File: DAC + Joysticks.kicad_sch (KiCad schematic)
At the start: 105 parts, among them J10 L Phono, J11 R Phono, J8 JOY0, J9 JOY1, U23 74HC374, U24 74HC374, U25 74LS244, U26 74LS244, U27 74LS373, U28 74LS244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

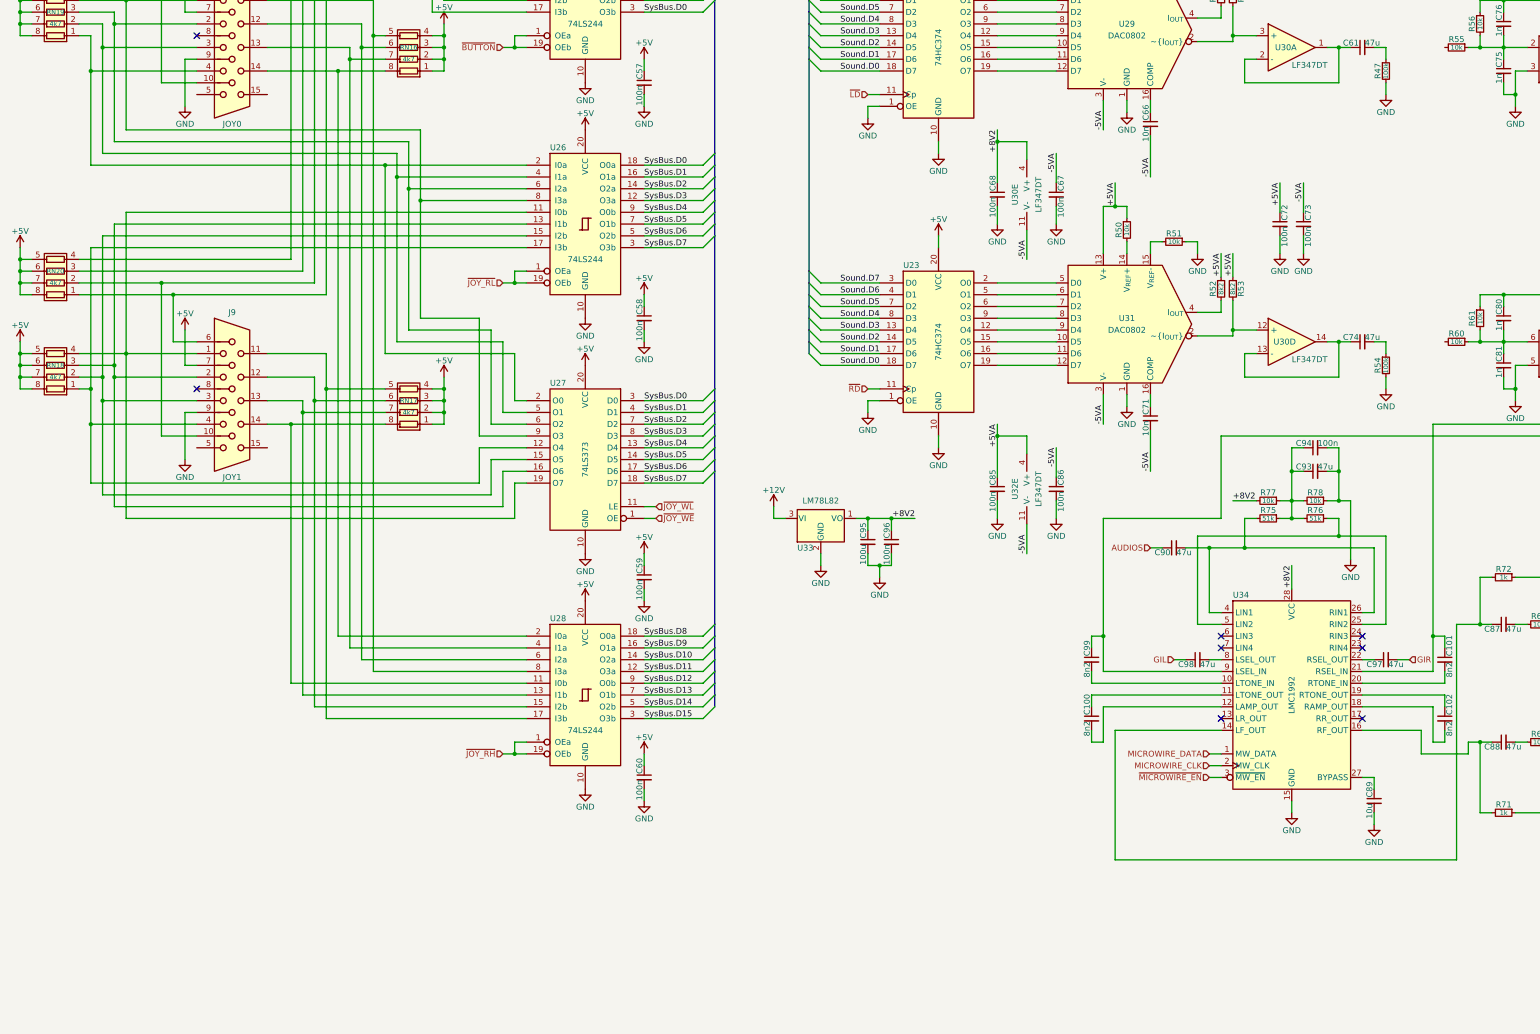
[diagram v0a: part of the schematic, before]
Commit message: motherboard: Added the circuitry for the joystick pads
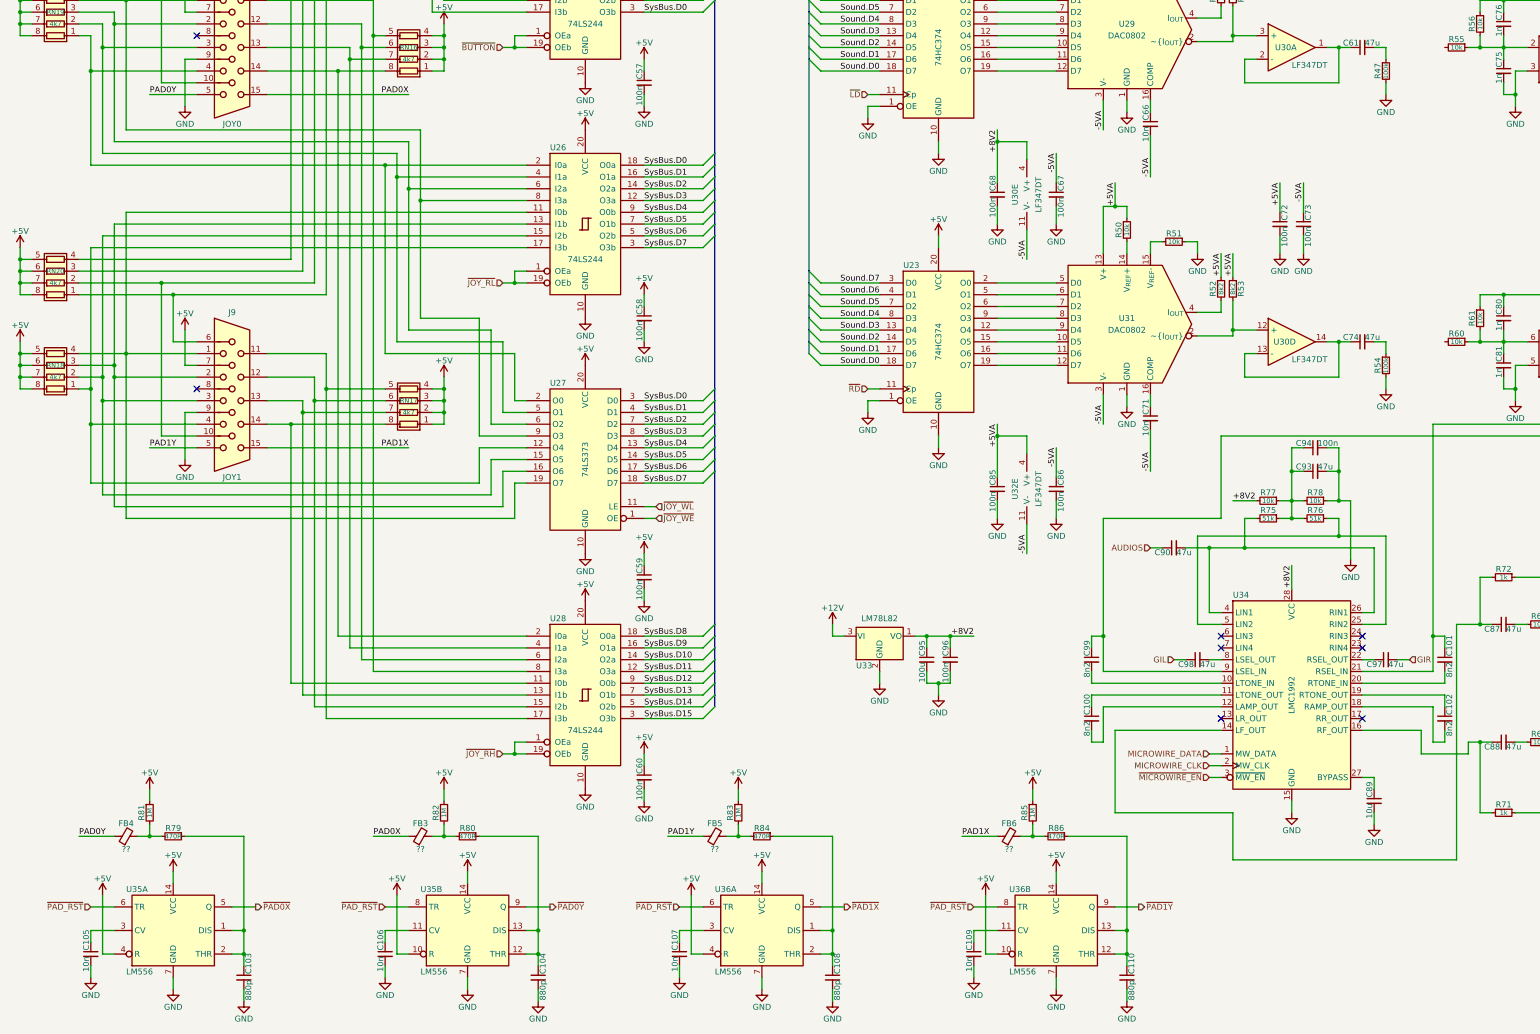
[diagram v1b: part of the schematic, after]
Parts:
- added C103, C104, C108, C110: 880p, rhais_rcl:C0603, symbol Device:C_Small
- added C105, C106, C107, C109: 10n, rhais_rcl:C0603, symbol Device:C_Small
- added FB3, FB4, FB5, FB6: ??, symbol Device:FerriteBead_Small
- added R79, R80, R84, R86: 470R, rhais_rcl:R0603, symbol Device:R_Small
- added R81, R82, R83, R85: 1M, rhais_rcl:R0603, symbol Device:R_Small
- added U35, U36: LM556, symbol Timer:LM556
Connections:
- net +5V: now also R81.1, R82.1, R83.1, R85.1, U35.10 (R), U35.14 (VCC), U35.14 (VCC), U35.4 (R), U36.10 (R), U36.14 (VCC), U36.14 (VCC), U36.4 (R)
- net GND: now also C103.2, C104.2, C105.2, C106.2, C107.2, C108.2, C109.2, C110.2, U35.7 (GND), U35.7 (GND), U36.7 (GND), U36.7 (GND)
- net PAD0X: now reaches J8.15
- net PAD0X: now also FB3.1
- net PAD0Y: now reaches J8.5
- net PAD0Y: now also FB4.1
- net PAD1X: now reaches J9.15
- net PAD1X: now also FB6.1
- net PAD1Y: now reaches J9.5
- net PAD1Y: now also FB5.1
- new net: C110.1, R86.1, U36.12 (THR), U36.13 (DIS)
- new net: C103.1, R79.1, U35.1 (DIS), U35.2 (THR)
- new net: C104.1, R80.1, U35.12 (THR), U35.13 (DIS)
- new net: FB3.2, R80.2, R82.2
- new net: C108.1, R84.1, U36.1 (DIS), U36.2 (THR)
- new net: FB5.2, R83.2, R84.2
- new net: FB4.2, R79.2, R81.2
- new net: C106.1, U35.11 (CV)
- new net: C109.1, U36.11 (CV)
- new net: FB6.2, R85.2, R86.2
- new net: C107.1, U36.3 (CV)
- new net: C105.1, U35.3 (CV)
- new net ~{PAD0X}: U35.5 (Q)
- new net ~{PAD0Y}: U35.9 (Q)
- new net ~{PAD1X}: U36.5 (Q)
- new net ~{PAD1Y}: U36.9 (Q)
- new net ~{PAD_RST}: U35.6 (TR), U35.8 (TR), U36.6 (TR), U36.8 (TR)
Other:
- moved on the sheet: C95, C96, U33

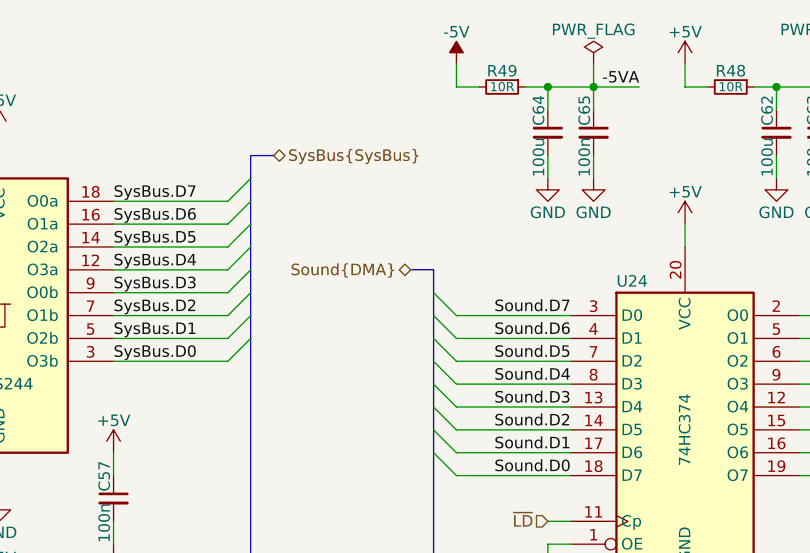
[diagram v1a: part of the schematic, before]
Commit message: motherboard: Added SHIFTER to the schematic and tidied up a pile
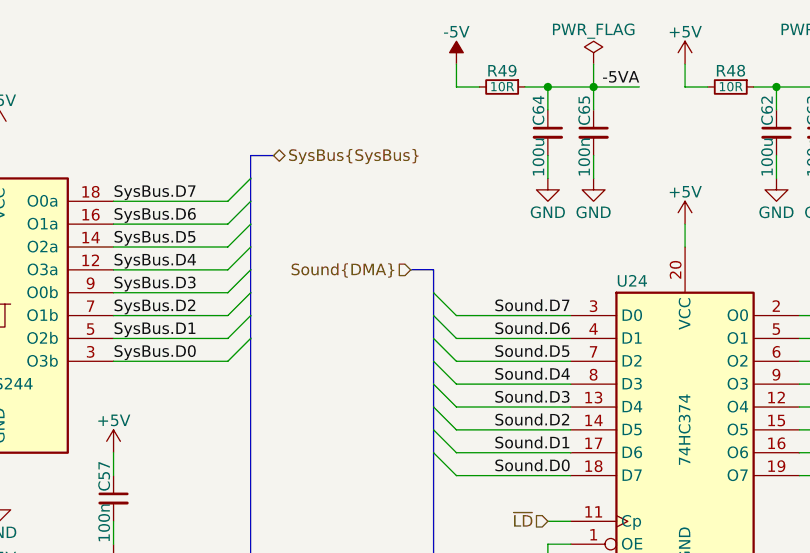
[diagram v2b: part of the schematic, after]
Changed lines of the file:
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@@
 	)
 	(hierarchical_label "Sound{DMA}"
-		(shape bidirectional)
+		(shape input)
 		(at 185.42 45.72 180)
 		(effects

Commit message: motherboard: Schematic cleanup in the peripherals sections
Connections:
- net ~{PAD_RST} renamed ~{PAD_RESET}
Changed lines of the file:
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@@
 	(wire
 		(pts
-			(xy 266.7 195.58) (xy 269.24 195.58)
+			(xy 264.16 195.58) (xy 269.24 195.58)
 		)
 		(stroke
@@
 	(wire
 		(pts
-			(xy 370.84 134.62) (xy 370.84 137.16)
+			(xy 370.84 134.62) (xy 370.84 139.7)
 		)
 		(stroke
@@
 	(wire
 		(pts
-			(xy 314.96 195.58) (xy 317.5 195.58)
+			(xy 314.96 195.58) (xy 320.04 195.58)
 		)
 		(stroke
@@
 	(wire
 		(pts
-			(xy 370.84 71.12) (xy 370.84 73.66)
+			(xy 370.84 71.12) (xy 370.84 76.2)
 		)
 		(stroke
@@
 		)
 	)
+	(label "GIR"
+		(at 320.04 195.58 180)
+		(effects
+			(font
+				(size 1.27 1.27)
+			)
+			(justify right bottom)
+		)
+	)
+	(label "GIL"
+		(at 264.16 195.58 0)
+		(effects
+			(font
+				(size 1.27 1.27)
+			)
+			(justify left bottom)
+		)
+	)
 	(label "-5VA"
 		(at 251.46 81.28 90)
@@
 		)
 	)
+	(label "GIL"
+		(at 370.84 76.2 90)
+		(effects
+			(font
+				(size 1.27 1.27)
+			)
+			(justify left bottom)
+		)
+	)
 	(label "+8V2"
 		(at 279.4 161.29 0)
@@
 		)
 	)
+	(label "GIR"
+		(at 370.84 139.7 90)
+		(effects
+			(font
+				(size 1.27 1.27)
+			)
+			(justify left bottom)
+		)
+	)
 	(hierarchical_label "SysBus{SysBus}"
 		(shape bidirectional)
@@
 		)
 	)
-	(hierarchical_label "GIR"
-		(shape input)
-		(at 317.5 195.58 0)
-		(effects
-			(font
-				(size 1.27 1.27)
-			)
-			(justify left)
-		)
-	)
 	(hierarchical_label "MICROWIRE_DATA"
 		(shape input)
@@
 		)
 	)
-	(hierarchical_label "GIL"
-		(shape input)
-		(at 266.7 195.58 180)
-		(effects
-			(font
-				(size 1.27 1.27)
-			)
-			(justify right)
-		)
-	)
-	(hierarchical_label "~{PAD_RST}"
+	(hierarchical_label "~{PAD_RESET}"
 		(shape input)
 		(at 160.02 248.92 180)
@@
 		)
 	)
-	(hierarchical_label "~{PAD_RST}"
+	(hierarchical_label "~{PAD_RESET}"
 		(shape input)
 		(at 96.52 248.92 180)
@@
 		)
 	)
-	(hierarchical_label "GIL"
-		(shape input)
-		(at 370.84 73.66 270)
-		(effects
-			(font
-				(size 1.27 1.27)
-			)
-			(justify right)
-		)
-	)
 	(hierarchical_label "MICROWIRE_CLK"
 		(shape input)
@@
 		)
 	)
-	(hierarchical_label "GIR"
-		(shape input)
-		(at 370.84 137.16 270)
-		(effects
-			(font
-				(size 1.27 1.27)
-			)
-			(justify right)
-		)
-	)
-	(hierarchical_label "~{PAD_RST}"
+	(hierarchical_label "~{PAD_RESET}"
 		(shape input)
 		(at 223.52 248.92 180)
@@
 		)
 	)
-	(hierarchical_label "~{PAD_RST}"
+	(hierarchical_label "~{PAD_RESET}"
 		(shape input)
 		(at 33.02 248.92 180)

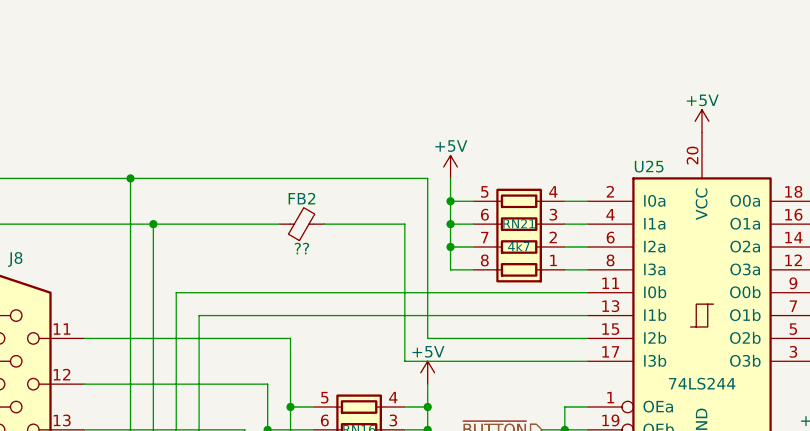
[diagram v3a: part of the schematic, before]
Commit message: motherboard: More signal routing, and starting in on the BoM
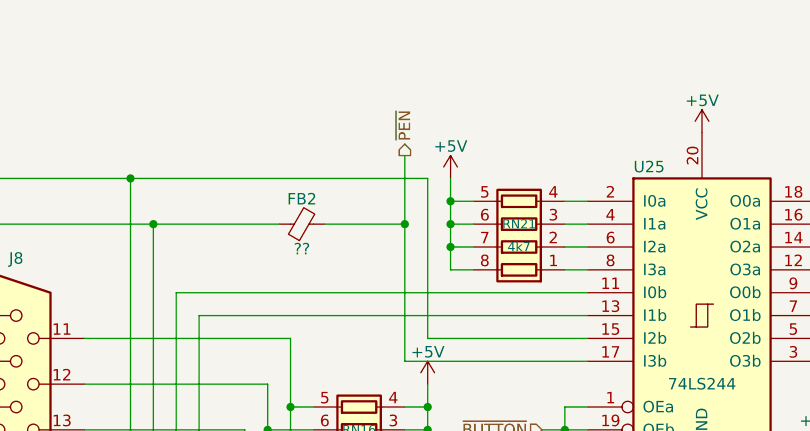
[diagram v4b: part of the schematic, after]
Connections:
- net ~{PEN}: now reaches FB2.2, U25.17 (I3b)

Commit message: motherboard: Begun routing the internal floppy disk interface
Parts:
- U30, U32: footprint Package_SO:SO-14_3.9x8.65mm_P1.27mm -> rhais_package-smd:SO-14_3.9x8.65mm_P1.27mm
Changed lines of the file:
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@@
 			)
 		)
-		(property "Footprint" "Package_SO:SO-14_3.9x8.65mm_P1.27mm"
+		(property "Footprint" "rhais_package-smd:SO-14_3.9x8.65mm_P1.27mm"
 			(at 237.49 158.75 0)
 			(effects
@@
 			)
 		)
-		(property "Footprint" "Package_SO:SO-14_3.9x8.65mm_P1.27mm"
+		(property "Footprint" "rhais_package-smd:SO-14_3.9x8.65mm_P1.27mm"
 			(at 292.1 63.5 0)
 			(effects
@@
 			)
 		)
-		(property "Footprint" "Package_SO:SO-14_3.9x8.65mm_P1.27mm"
+		(property "Footprint" "rhais_package-smd:SO-14_3.9x8.65mm_P1.27mm"
 			(at 360.68 215.9 0)
 			(effects
@@
 			)
 		)
-		(property "Footprint" "Package_SO:SO-14_3.9x8.65mm_P1.27mm"
+		(property "Footprint" "rhais_package-smd:SO-14_3.9x8.65mm_P1.27mm"
 			(at 292.1 127 0)
 			(effects
@@
 			)
 		)
-		(property "Footprint" "Package_SO:SO-14_3.9x8.65mm_P1.27mm"
+		(property "Footprint" "rhais_package-smd:SO-14_3.9x8.65mm_P1.27mm"
 			(at 360.68 190.5 0)
 			(effects
@@
 			)
 		)
-		(property "Footprint" "Package_SO:SO-14_3.9x8.65mm_P1.27mm"
+		(property "Footprint" "rhais_package-smd:SO-14_3.9x8.65mm_P1.27mm"
 			(at 350.52 129.54 0)
 			(effects
@@
 			)
 		)
-		(property "Footprint" "Package_SO:SO-14_3.9x8.65mm_P1.27mm"
+		(property "Footprint" "rhais_package-smd:SO-14_3.9x8.65mm_P1.27mm"
 			(at 237.49 95.25 0)
 			(effects
@@
 			)
 		)
-		(property "Footprint" "Package_SO:SO-14_3.9x8.65mm_P1.27mm"
+		(property "Footprint" "rhais_package-smd:SO-14_3.9x8.65mm_P1.27mm"
 			(at 388.62 129.54 0)
 			(effects
@@
 			)
 		)
-		(property "Footprint" "Package_SO:SO-14_3.9x8.65mm_P1.27mm"
+		(property "Footprint" "rhais_package-smd:SO-14_3.9x8.65mm_P1.27mm"
 			(at 388.62 66.04 0)
 			(effects
@@
 			)
 		)
-		(property "Footprint" "Package_SO:SO-14_3.9x8.65mm_P1.27mm"
+		(property "Footprint" "rhais_package-smd:SO-14_3.9x8.65mm_P1.27mm"
 			(at 350.52 66.04 0)
 			(effects
